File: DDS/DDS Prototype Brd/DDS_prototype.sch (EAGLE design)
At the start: 31 parts, among them T1 ADTT1-6+, U1 AD9913, U2 S-1711A1818-I6T1U, Y1 TSX-3225 25.0000MF10P-C0

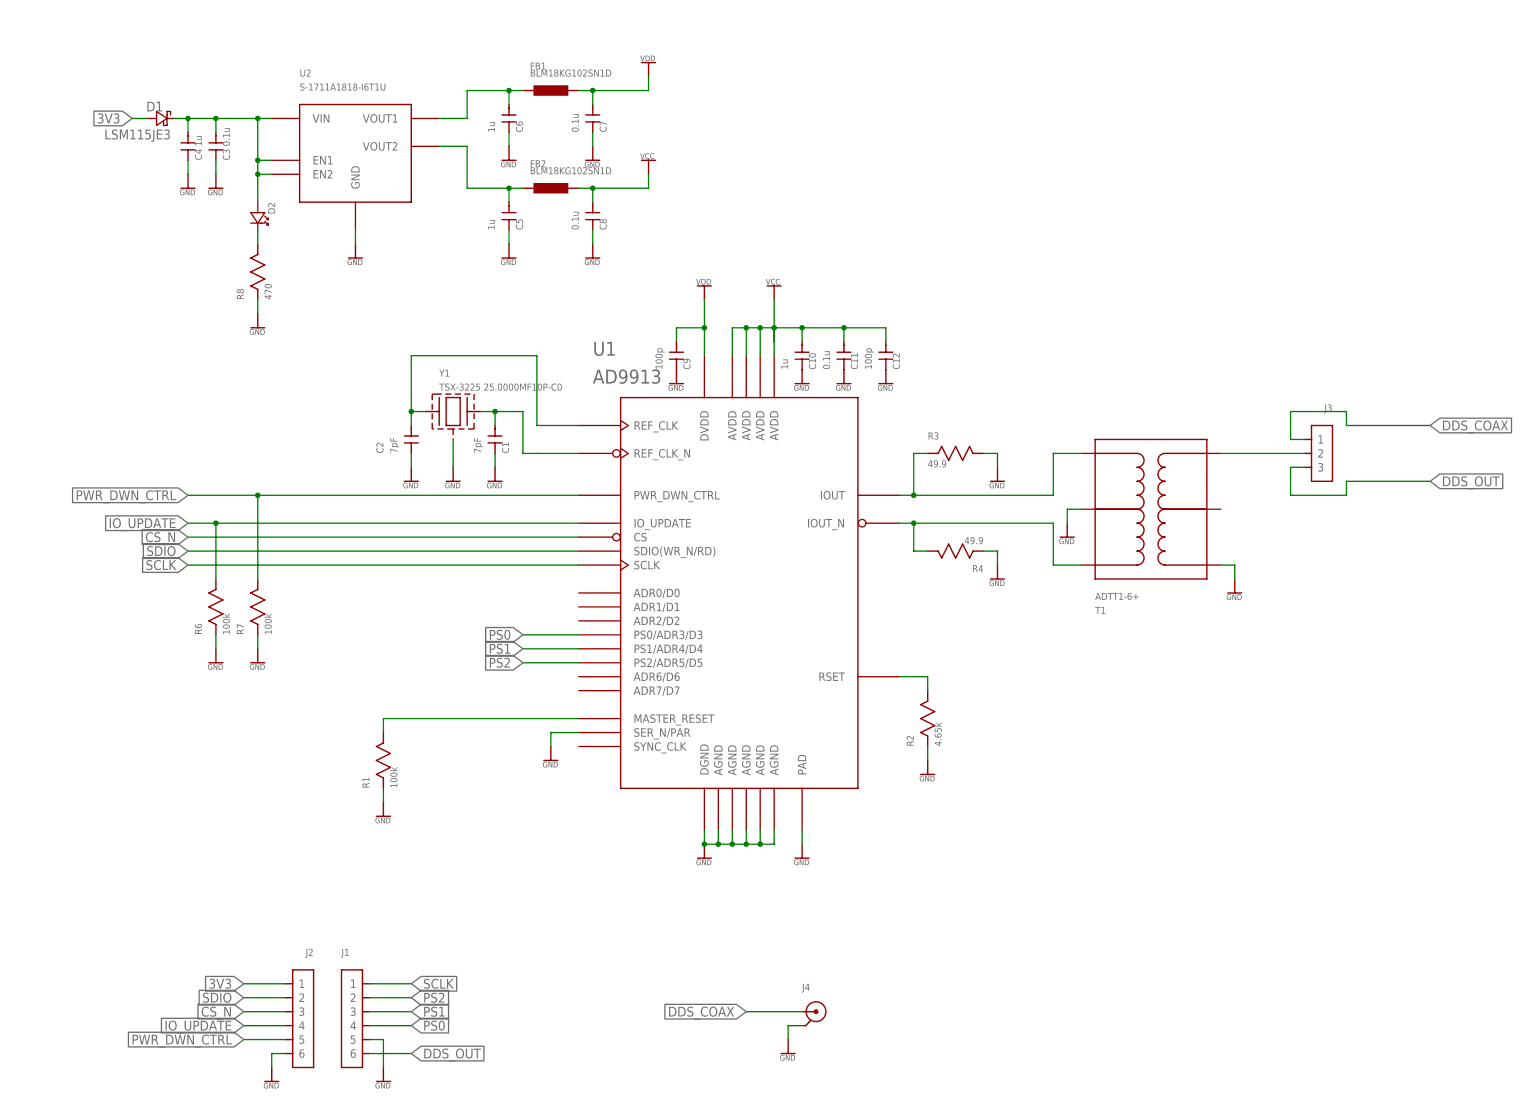
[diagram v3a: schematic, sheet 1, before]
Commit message: updated board, now has all 3d models, libraried are now managed libs only
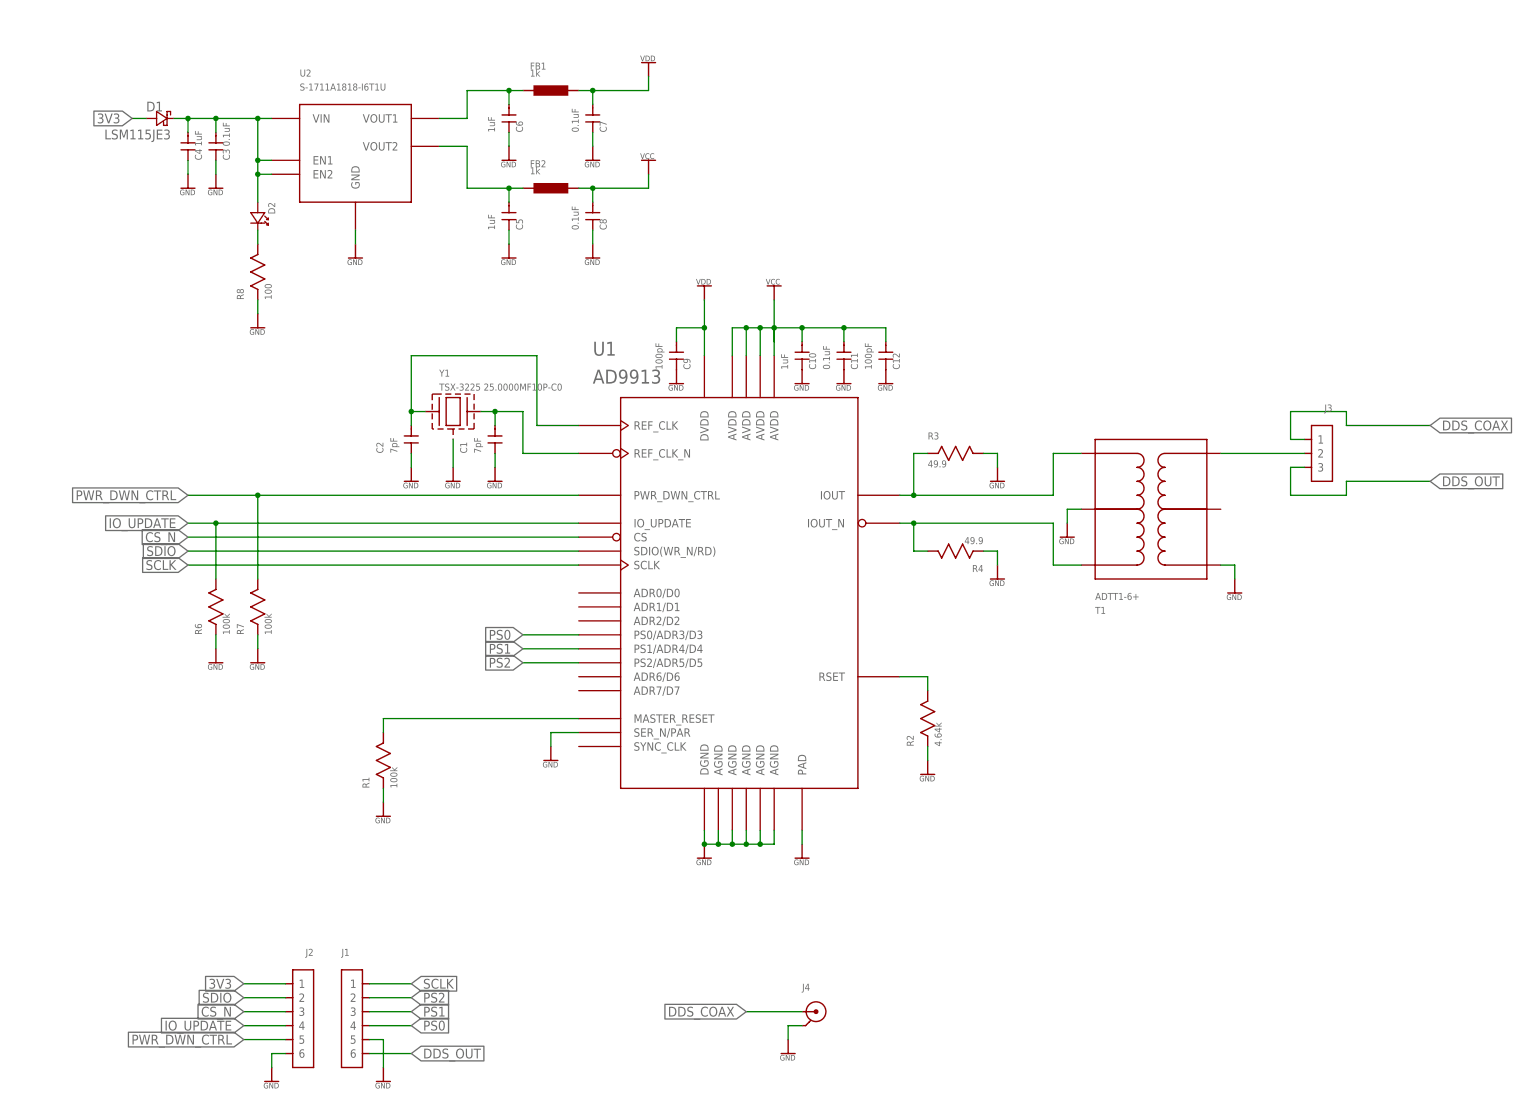
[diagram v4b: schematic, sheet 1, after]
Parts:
- C1, C2: device Capacitors:0402_CAP -> Capacitors:CC0402DRNPO9BN7R0
- C10, C4, C5, C6: value 1u -> 1uF; device Capacitors:0402_CAP -> Capacitors:CC0402KRX5R7BB105
- C11, C3, C7, C8: value 0.1u -> 0.1uF; device Capacitors:0402_CAP -> Capacitors:CC0402KRX5R7BB104
- C12, C9: value 100p -> 100pF; device Capacitors:0402_CAP -> Capacitors:CC0402JRNPO9BN101
- D1: device Diodes:SCHOTTKEY -> Diodes:LSM115JE3/TR13
- D2: device Diodes:LED -> Diodes:QBLP595-IG
- FB1, FB2: value BLM18KG102SN1D -> 1k; device Inductors:0603_FB -> Inductors:BLM18KG102SN1D
- R1, R6, R7: device Resistors:RESISTOR0402 -> Resistors:RC0402JR-07100KL
- R2: value 4.65k -> 4.64k; device Resistors:RESISTOR0402 -> Resistors:RC0402FR-074K64L
- R3, R4: device Resistors:0402_RESISTOR -> Resistors:RC0402FR-0749R9L
- R8: value 470 -> 100; device Resistors:RESISTOR0402 -> Resistors:RC0402JR-07100RL
- Y1: device Crystals:TSX-3225 -> Crystals:TSX-322525.0000MF10P-C0
